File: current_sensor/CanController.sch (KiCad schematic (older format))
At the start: 43 parts, among them P10 CONN_02X03, P7 CONN_01X03, P8 USB, P9 CONN_01X02, SW1 RESET, SW2 BOOT, U6 STM32F042C6, U7 mcp2562

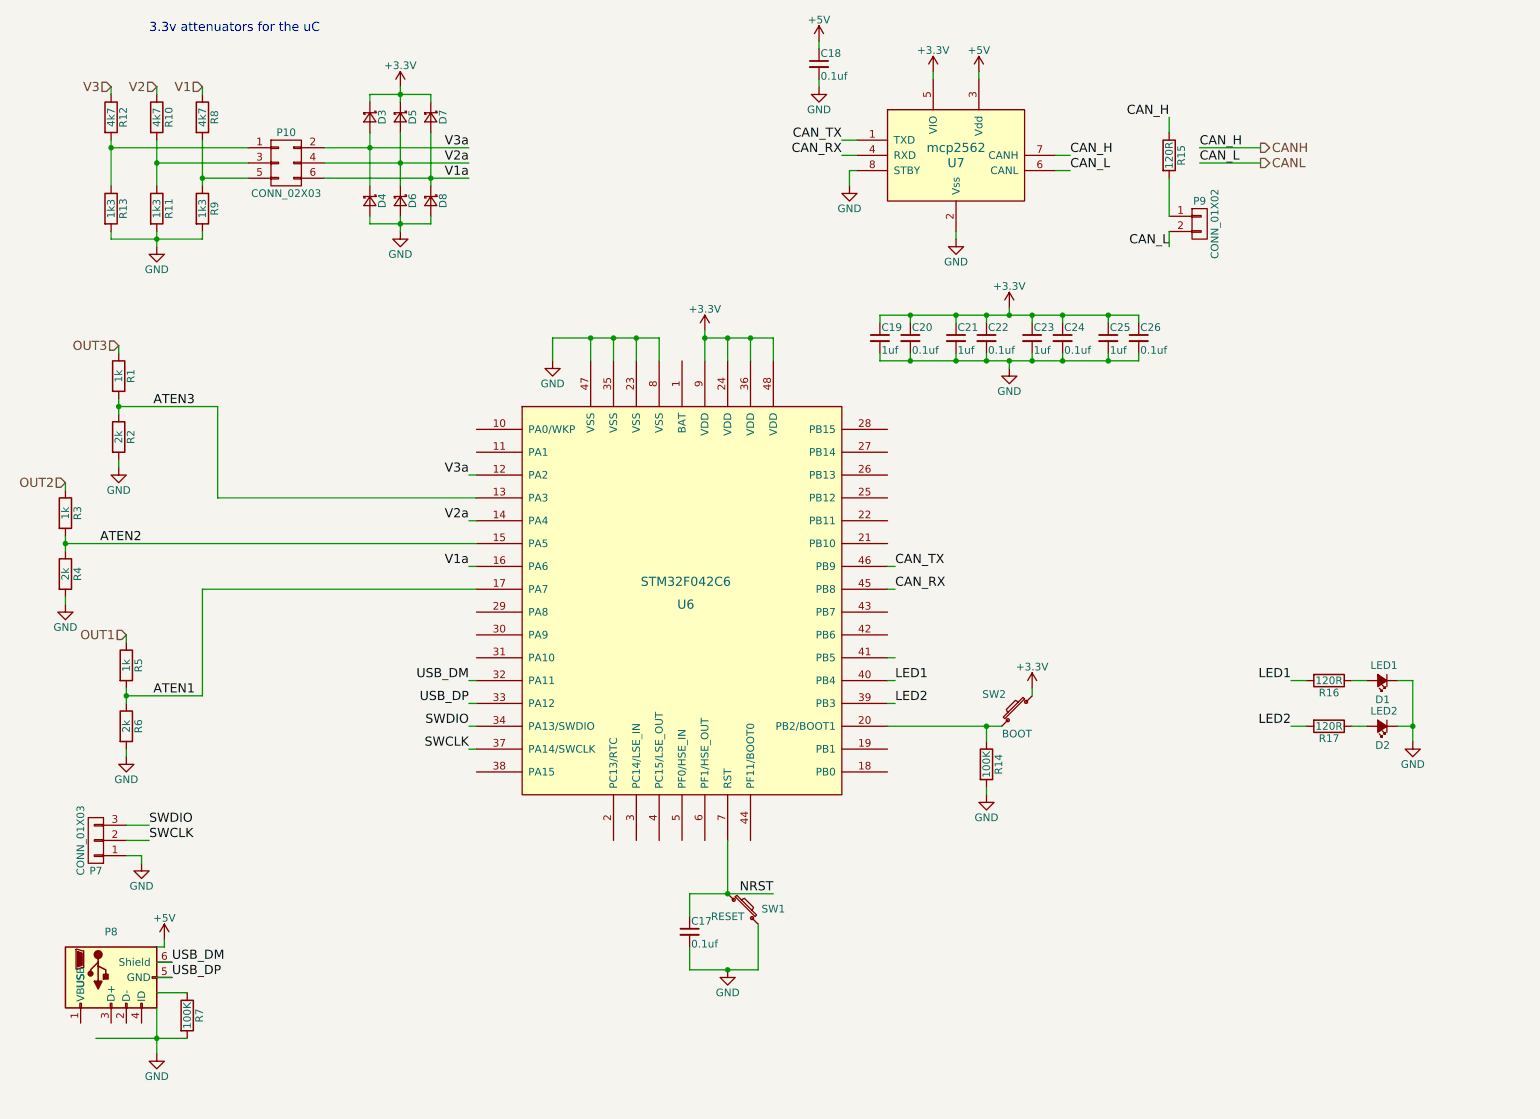
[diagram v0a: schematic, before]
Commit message: Added all components to the board and finilized placement
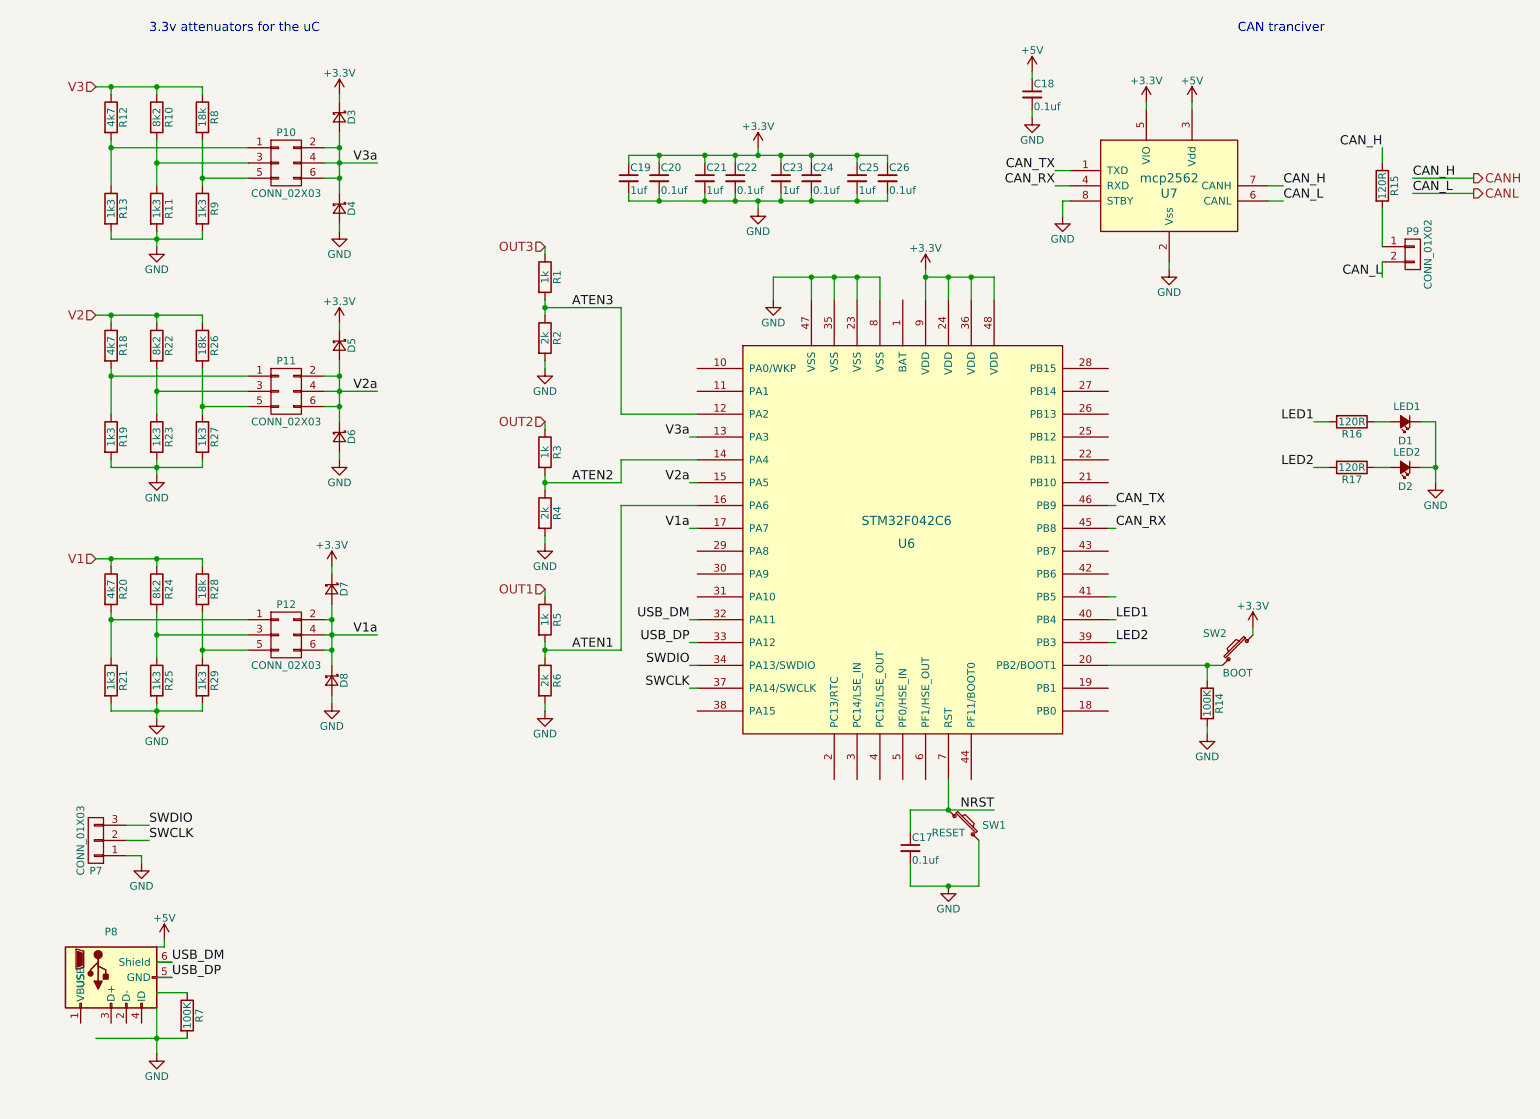
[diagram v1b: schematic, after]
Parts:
- added P11, P12: CONN_02X03, Pin_Headers:Pin_Header_Straight_2x03, symbol CONN_02X03
- added R18, R20: 4k7, Resistors_SMD:R_0603_HandSoldering, symbol R
- added R19, R21, R23, R25, R27, R29: 1k3, Resistors_SMD:R_0603_HandSoldering, symbol R
- added R22, R24: 8k2, Resistors_SMD:R_0603_HandSoldering, symbol R
- added R26, R28: 18k, Resistors_SMD:R_0603_HandSoldering, symbol R
- R10: value 4k7 -> 8k2
- R8: value 4k7 -> 18k; Distributor (none) -> Mouser
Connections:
- wire segments 130 -> 227
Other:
- note added: "CAN tranciver"
- moved on the sheet: C17, C18, C19, C20, C21, C22, C23, C24, C25, C26, D1, D2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

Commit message: added more silkscreen text
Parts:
- D3, D4, D5, D6, D7, D8: Distributor (none) -> Mouser; PN (none) -> 512-SS14FL
- SW1, SW2: footprint Buttons_Switches_SMD:SW_SPST_EVQP0 -> Buttons_Switches_ThroughHole:SW_PUSH_6mm
- U6: Distributor (none) -> Mouser; PN (none) -> 511-STM32F042C6T6
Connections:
- wire segments 227 -> 165
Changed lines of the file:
@@
 F 0 "SW2" H 8650 4960 50  0000 C CNN
 F 1 "BOOT" H 8500 4700 50  0000 C CNN
-F 2 "Buttons_Switches_SMD:SW_SPST_EVQP0" V 8500 4850 50  0001 C CNN
+F 2 "Buttons_Switches_ThroughHole:SW_PUSH_6mm" V 8500 4850 50  0001 C CNN
 F 3 "" H 8500 4850 50  0000 C CNN
 	1    8500 4850
@@
 F 0 "SW1" H 6900 6000 50  0000 C CNN
 F 1 "RESET" H 6600 5950 50  0000 C CNN
-F 2 "Buttons_Switches_SMD:SW_SPST_EVQP0" H 6700 6000 50  0001 C CNN
+F 2 "Buttons_Switches_ThroughHole:SW_PUSH_6mm" H 6700 6000 50  0001 C CNN
 F 3 "" H 6700 6000 50  0000 C CNN
 	1    6700 6000
@@
 F 2 "Housings_QFP:TQFP-48_7x7mm_Pitch0.5mm" H 6300 4100 60  0001 C CNN
 F 3 "" H 6300 4100 60  0000 C CNN
+F 4 "Mouser" H 6300 4100 60  0001 C CNN "Distributor"
+F 5 "511-STM32F042C6T6 " H 6300 4100 60  0001 C CNN "PN"
 	1    6300 4100
 	1    0    0    -1
@@
 F 2 "Diodes_SMD:SOD-123" V 2600 1950 50  0001 C CNN
 F 3 "" V 2600 1950 50  0000 C CNN
+F 4 "Mouser" H 2600 1950 60  0001 C CNN "Distributor"
+F 5 "512-SS14FL " H 2600 1950 60  0001 C CNN "PN"
 	1    2600 1950
 	0    1    1    0
@@
 F 2 "Diodes_SMD:SOD-123" V 2600 1350 50  0001 C CNN
 F 3 "" V 2600 1350 50  0000 C CNN
+F 4 "Mouser" H 2600 1350 60  0001 C CNN "Distributor"
+F 5 "512-SS14FL " H 2600 1350 60  0001 C CNN "PN"
 	1    2600 1350
 	0    1    1    0
@@
 F 2 "Diodes_SMD:SOD-123" V 2600 2850 50  0001 C CNN
 F 3 "" V 2600 2850 50  0000 C CNN
+F 4 "Mouser" H 2600 2850 60  0001 C CNN "Distributor"
+F 5 "512-SS14FL " H 2600 2850 60  0001 C CNN "PN"
 	1    2600 2850
 	0    1    1    0
 $EndComp
 Wire Wire Line
-	6450 2350 6450 2400
-Wire Wire Line
-	6450 2400 6450 2550
-Wire Wire Line
-	6450 2400 6600 2400
-Wire Wire Line
-	6600 2400 6750 2400
-Wire Wire Line
-	6750 2400 6900 2400
+	6450 2350 6450 2550
+Wire Wire Line
+	6450 2400 6900 2400
 Connection ~ 6450 2400
 Wire Wire Line
@@
 	9700 3350 9800 3350
 Wire Wire Line
-	9800 3350 9800 3650
-Wire Wire Line
-	9800 3650 9800 3750
+	9800 3350 9800 3750
 Wire Wire Line
 	9800 3650 9700 3650
@@
 	1450 6800 1400 6800
 Wire Wire Line
-	1400 7200 1400 7400
-Wire Wire Line
-	1400 7400 1400 7500
-Wire Wire Line
-	1000 7400 1400 7400
-Wire Wire Line
-	1400 7400 1600 7400
+	1400 7200 1400 7500
+Wire Wire Line
+	1000 7400 1600 7400
 Connection ~ 1400 7400
 Wire Wire Line
@@
 	6350 6250 6350 6400
 Wire Wire Line
-	7650 4950 8300 4950
-Wire Wire Line
-	8300 4950 8400 4950
+	7650 4950 8400 4950
 Wire Wire Line
 	8300 5050 8300 4950
@@
 	6000 1600 6000 1650
 Wire Wire Line
-	6350 5900 6600 5900
-Wire Wire Line
-	6600 5900 6900 5900
+	6350 5900 6900 5900
 Wire Wire Line
 	6200 1600 6200 1650
@@
 	5450 2550 5450 2400
 Wire Wire Line
-	5450 2400 5700 2400
-Wire Wire Line
-	5700 2400 5850 2400
-Wire Wire Line
-	5850 2400 6000 2400
-Wire Wire Line
-	6000 2400 6150 2400
+	5450 2400 6150 2400
 Wire Wire Line
 	5700 2400 5700 2550
@@
 	6800 6400 6800 6100
 Wire Wire Line
-	6350 6400 6600 6400
-Wire Wire Line
-	6600 6400 6800 6400
+	6350 6400 6800 6400
 Connection ~ 6600 6400
 Wire Wire Line
@@
 	4500 1650 4500 1600
 Wire Wire Line
-	4500 1600 4700 1600
-Wire Wire Line
-	4700 1600 5000 1600
-Wire Wire Line
-	5000 1600 5200 1600
-Wire Wire Line
-	5200 1600 5350 1600
-Wire Wire Line
-	5350 1600 5500 1600
-Wire Wire Line
-	5500 1600 5700 1600
-Wire Wire Line
-	5700 1600 6000 1600
-Wire Wire Line
-	6000 1600 6200 1600
+	4500 1600 6200 1600
 Wire Wire Line
 	4700 1650 4700 1600
@@
 	6200 1900 6200 1850
 Wire Wire Line
-	4500 1900 4700 1900
-Wire Wire Line
-	4700 1900 5000 1900
-Wire Wire Line
-	5000 1900 5200 1900
-Wire Wire Line
-	5200 1900 5350 1900
-Wire Wire Line
-	5350 1900 5500 1900
-Wire Wire Line
-	5500 1900 5700 1900
-Wire Wire Line
-	5700 1900 6000 1900
-Wire Wire Line
-	6000 1900 6200 1900
+	4500 1900 6200 1900
 Wire Wire Line
 	4500 1900 4500 1850
@@
 	3950 2250 3950 2200
 Wire Wire Line
-	3950 2550 3950 2600
-Wire Wire Line
-	3950 2600 3950 2650
+	3950 2550 3950 2650
 Wire Wire Line
 	3950 2950 3950 3000
@@
 	3950 3400 3950 3350
 Wire Wire Line
-	3950 3700 3950 3750
-Wire Wire Line
-	3950 3750 3950 3800
+	3950 3700 3950 3800
 Wire Wire Line
 	3950 4100 3950 4150
@@
 	3950 4500 3950 4450
 Wire Wire Line
-	3950 4800 3950 4850
-Wire Wire Line
-	3950 4850 3950 4900
+	3950 4800 3950 4900
 Wire Wire Line
 	3950 5200 3950 5250
@@
 	1100 2100 1100 2150
 Wire Wire Line
-	1400 2100 1400 2150
-Wire Wire Line
-	1400 2150 1400 2200
+	1400 2100 1400 2200
 Wire Wire Line
 	1700 1150 1700 1200
@@
 F 2 "Diodes_SMD:SOD-123" V 2550 4450 50  0001 C CNN
 F 3 "" V 2550 4450 50  0000 C CNN
+F 4 "Mouser" H 2550 4450 60  0001 C CNN "Distributor"
+F 5 "512-SS14FL " H 2550 4450 60  0001 C CNN "PN"
 	1    2550 4450
 	0    1    1    0
@@
 	4450 2600 4450 3300
 Wire Wire Line
-	1100 2150 1400 2150
-Wire Wire Line
-	1400 2150 1700 2150
+	1100 2150 1700 2150
 Connection ~ 1400 2150
 Wire Wire Line
-	1100 1500 1100 1550
-Wire Wire Line
-	1100 1550 1100 1800
-Wire Wire Line
-	1400 1500 1400 1650
-Wire Wire Line
-	1400 1650 1400 1800
-Wire Wire Line
-	1700 1500 1700 1750
-Wire Wire Line
-	1700 1750 1700 1800
+	1100 1500 1100 1800
+Wire Wire Line
+	1400 1500 1400 1800
+Wire Wire Line
+	1700 1500 1700 1800
 Wire Wire Line
 	1100 1550 2000 1550
@@
 	1400 2650 1400 2700
 Wire Wire Line
-	1400 3600 1400 3650
-Wire Wire Line
-	1400 3650 1400 3700
+	1400 3600 1400 3700
 Wire Wire Line
 	1700 2650 1700 2700
@@
 $EndComp
 Wire Wire Line
-	1100 3650 1400 3650
-Wire Wire Line
-	1400 3650 1700 3650
+	1100 3650 1700 3650
 Connection ~ 1400 3650
 Wire Wire Line
-	1100 3000 1100 3050
-Wire Wire Line
-	1100 3050 1100 3300
-Wire Wire Line
-	1400 3000 1400 3150
-Wire Wire Line
-	1400 3150 1400 3300
-Wire Wire Line
-	1700 3000 1700 3250
-Wire Wire Line
-	1700 3250 1700 3300
+	1100 3000 1100 3300
+Wire Wire Line
+	1400 3000 1400 3300
+Wire Wire Line
+	1700 3000 1700 3300
 Wire Wire Line
 	1100 3050 2000 3050
@@
 	1400 4250 1400 4300
 Wire Wire Line
-	1400 5200 1400 5250
-Wire Wire Line
-	1400 5250 1400 5300
+	1400 5200 1400 5300
 Wire Wire Line
 	1700 4250 1700 4300
@@
 $EndComp
 Wire Wire Line
-	1100 5250 1400 5250
-Wire Wire Line
-	1400 5250 1700 5250
+	1100 5250 1700 5250
 Connection ~ 1400 5250
 Wire Wire Line
-	1100 4600 1100 4650
-Wire Wire Line
-	1100 4650 1100 4900
-Wire Wire Line
-	1400 4600 1400 4750
-Wire Wire Line
-	1400 4750 1400 4900
-Wire Wire Line
-	1700 4600 1700 4850
-Wire Wire Line
-	1700 4850 1700 4900
+	1100 4600 1100 4900
+Wire Wire Line
+	1400 4600 1400 4900
+Wire Wire Line
+	1700 4600 1700 4900
 Wire Wire Line
 	1100 4650 2000 4650
@@
 Connection ~ 1700 4850
 Wire Wire Line
-	1000 1150 1100 1150
-Wire Wire Line
-	1100 1150 1400 1150
-Wire Wire Line
-	1400 1150 1700 1150
+	1000 1150 1700 1150
 Connection ~ 1400 1150
 Wire Wire Line
@@
 F 2 "Diodes_SMD:SOD-123" V 2600 3450 50  0001 C CNN
 F 3 "" V 2600 3450 50  0000 C CNN
+F 4 "Mouser" H 2600 3450 60  0001 C CNN "Distributor"
+F 5 "512-SS14FL " H 2600 3450 60  0001 C CNN "PN"
 	1    2600 3450
 	0    1    1    0
@@
 F 2 "Diodes_SMD:SOD-123" V 2550 5050 50  0001 C CNN
 F 3 "" V 2550 5050 50  0000 C CNN
+F 4 "Mouser" H 2550 5050 60  0001 C CNN "Distributor"
+F 5 "512-SS14FL " H 2550 5050 60  0001 C CNN "PN"
 	1    2550 5050
 	0    1    1    0
 $EndComp
 Wire Wire Line
-	2500 4750 2550 4750
-Wire Wire Line
-	2550 4750 2850 4750
+	2500 4750 2850 4750
 Wire Wire Line
 	2550 4300 2550 4350
@@
 	2550 4850 2500 4850
 Wire Wire Line
-	2550 4550 2550 4650
-Wire Wire Line
-	2550 4650 2550 4750
-Wire Wire Line
-	2550 4750 2550 4850
-Wire Wire Line
-	2550 4850 2550 4950
+	2550 4550 2550 4950
 Connection ~ 2550 4750
 Wire Wire Line
@@
 Connection ~ 2550 4650
 Wire Wire Line
-	1000 4250 1100 4250
-Wire Wire Line
-	1100 4250 1400 4250
-Wire Wire Line
-	1400 4250 1700 4250
+	1000 4250 1700 4250
 Connection ~ 1100 4250
 Connection ~ 1400 4250
 Wire Wire Line
-	2600 2950 2600 3050
-Wire Wire Line
-	2600 3050 2600 3150
-Wire Wire Line
-	2600 3150 2600 3250
-Wire Wire Line
-	2600 3250 2600 3350
+	2600 2950 2600 3350
 Connection ~ 2600 3250
 Connection ~ 2600 3050
@@
 	2500 3250 2600 3250
 Wire Wire Line
-	2500 3150 2600 3150
-Wire Wire Line
-	2600 3150 2850 3150
+	2500 3150 2850 3150
 Wire Wire Line
 	2500 3050 2600 3050
 Wire Wire Line
-	1000 2650 1100 2650
-Wire Wire Line
-	1100 2650 1400 2650
-Wire Wire Line
-	1400 2650 1700 2650
+	1000 2650 1700 2650
 Connection ~ 1100 2650
 Connection ~ 1400 2650
 Wire Wire Line
-	2600 1450 2600 1550
-Wire Wire Line
-	2600 1550 2600 1650
-Wire Wire Line
-	2600 1650 2600 1750
-Wire Wire Line
-	2600 1750 2600 1850
+	2600 1450 2600 1850
 Wire Wire Line
 	2500 1550 2600 1550
 Connection ~ 2600 1550
 Wire Wire Line
-	2500 1650 2600 1650
-Wire Wire Line
-	2600 1650 2850 1650
+	2500 1650 2850 1650
 Connection ~ 2600 1650
 Wire Wire Line

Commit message: fixed some stuff
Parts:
- SW1, SW2: Distributor (none) -> Mouser; PN (none) -> SKHHPPA010
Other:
- note added: "On chip debugger.\nUse a stm32Nucleo board or stlinkv2."
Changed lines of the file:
@@
 F 2 "Buttons_Switches_ThroughHole:SW_PUSH_6mm" V 8500 4850 50  0001 C CNN
 F 3 "" H 8500 4850 50  0000 C CNN
+F 4 "Mouser" H 8500 4850 60  0001 C CNN "Distributor"
+F 5 "SKHHPPA010 " H 8500 4850 60  0001 C CNN "PN"
 	1    8500 4850
 	-1   0    0    -1
@@
 F 2 "Buttons_Switches_ThroughHole:SW_PUSH_6mm" H 6700 6000 50  0001 C CNN
 F 3 "" H 6700 6000 50  0000 C CNN
+F 4 "Mouser" H 6700 6000 60  0001 C CNN "Distributor"
+F 5 "SKHHPPA010 " H 6700 6000 60  0001 C CNN "PN"
 	1    6700 6000
 	1    0    0    -1
@@
 Wire Wire Line
 	4950 4050 4900 4050
+Text Notes 825  5800 0    60   ~ 0
+On chip debugger.\nUse a stm32Nucleo board or stlinkv2.
 $EndSCHEMATC

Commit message: updated 1593BB-box footprint
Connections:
- wire segments 165 -> 169
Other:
- moved on the sheet: R14, SW2
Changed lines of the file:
@@
 L SW_PUSH_SMALL SW2
 U 1 1 581EFCF0
-P 8500 4850
-F 0 "SW2" H 8650 4960 50  0000 C CNN
-F 1 "BOOT" H 8500 4700 50  0000 C CNN
-F 2 "Buttons_Switches_ThroughHole:SW_PUSH_6mm" V 8500 4850 50  0001 C CNN
-F 3 "" H 8500 4850 50  0000 C CNN
-F 4 "Mouser" H 8500 4850 60  0001 C CNN "Distributor"
-F 5 "SKHHPPA010 " H 8500 4850 60  0001 C CNN "PN"
-	1    8500 4850
+P 7450 5800
+F 0 "SW2" H 7600 5910 50  0000 C CNN
+F 1 "BOOT" H 7450 5650 50  0000 C CNN
+F 2 "Buttons_Switches_ThroughHole:SW_PUSH_6mm" V 7450 5800 50  0001 C CNN
+F 3 "" H 7450 5800 50  0000 C CNN
+F 4 "Mouser" H 7450 5800 60  0001 C CNN "Distributor"
+F 5 "SKHHPPA010 " H 7450 5800 60  0001 C CNN "PN"
+	1    7450 5800
 	-1   0    0    -1
 $EndComp
@@
 L GND #PWR035
 U 1 1 581EFCF1
-P 8300 5400
-F 0 "#PWR035" H 8300 5150 50  0001 C CNN
-F 1 "GND" H 8300 5250 50  0000 C CNN
-F 2 "" H 8300 5400 50  0000 C CNN
-F 3 "" H 8300 5400 50  0000 C CNN
-	1    8300 5400
+P 7250 6350
+F 0 "#PWR035" H 7250 6100 50  0001 C CNN
+F 1 "GND" H 7250 6200 50  0000 C CNN
+F 2 "" H 7250 6350 50  0000 C CNN
+F 3 "" H 7250 6350 50  0000 C CNN
+	1    7250 6350
 	1    0    0    -1
 $EndComp
@@
 L +3.3V #PWR036
 U 1 1 581EFCF2
-P 8600 4700
-F 0 "#PWR036" H 8600 4550 50  0001 C CNN
-F 1 "+3.3V" H 8600 4840 50  0000 C CNN
-F 2 "" H 8600 4700 50  0000 C CNN
-F 3 "" H 8600 4700 50  0000 C CNN
-	1    8600 4700
+P 7550 5650
+F 0 "#PWR036" H 7550 5500 50  0001 C CNN
+F 1 "+3.3V" H 7550 5790 50  0000 C CNN
+F 2 "" H 7550 5650 50  0000 C CNN
+F 3 "" H 7550 5650 50  0000 C CNN
+	1    7550 5650
 	1    0    0    -1
 $EndComp
@@
 L R R14
 U 1 1 581EFCF7
-P 8300 5200
-F 0 "R14" V 8380 5200 50  0000 C CNN
-F 1 "100K" V 8300 5200 50  0000 C CNN
-F 2 "Resistors_SMD:R_0603_HandSoldering" H 8230 5200 50  0001 C CNN
-F 3 "" H 8300 5200 50  0000 C CNN
-F 4 "Mouser" V 8300 5200 60  0001 C CNN "Distributor"
-F 5 "71-CRCW0603-100K-E3" V 8300 5200 60  0001 C CNN "PN"
-	1    8300 5200
+P 7250 6150
+F 0 "R14" V 7350 6150 50  0000 C CNN
+F 1 "100K" V 7150 6150 50  0000 C CNN
+F 2 "Resistors_SMD:R_0603_HandSoldering" H 7180 6150 50  0001 C CNN
+F 3 "" H 7250 6150 50  0000 C CNN
+F 4 "Mouser" V 7250 6150 60  0001 C CNN "Distributor"
+F 5 "71-CRCW0603-100K-E3" V 7250 6150 60  0001 C CNN "PN"
+	1    7250 6150
 	1    0    0    -1
 $EndComp
@@
 	6350 6250 6350 6400
 Wire Wire Line
-	7650 4950 8400 4950
-Wire Wire Line
-	8300 5050 8300 4950
-Connection ~ 8300 4950
-Wire Wire Line
-	8300 5400 8300 5350
-Wire Wire Line
-	8600 4700 8600 4750
+	7250 6000 7250 5900
+Connection ~ 7250 5900
+Wire Wire Line
+	7250 6350 7250 6300
+Wire Wire Line
+	7550 5650 7550 5700
 Connection ~ 6600 5900
 Wire Wire Line
@@
 Text Notes 825  5800 0    60   ~ 0
 On chip debugger.\nUse a stm32Nucleo board or stlinkv2.
+Wire Wire Line
+	7350 5900 7025 5900
+Wire Wire Line
+	7025 5900 7025 5700
+Wire Wire Line
+	7025 5700 6750 5700
+$Comp
+L GND #PWR?
+U 1 1 58806A24
+P 8000 5025
+F 0 "#PWR?" H 8000 4775 50  0001 C CNN
+F 1 "GND" H 8000 4875 50  0000 C CNN
+F 2 "" H 8000 5025 50  0000 C CNN
+F 3 "" H 8000 5025 50  0000 C CNN
+	1    8000 5025
+	1    0    0    -1
+$EndComp
+Wire Wire Line
+	8000 5025 8000 4950
+Wire Wire Line
+	8000 4950 7650 4950
 $EndSCHEMATC

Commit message: updated wiring diagrams
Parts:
- P9: value CONN_01X02 -> Term
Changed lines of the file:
@@
 U 1 1 581EFCEC
 P 1100 7000
+AR Path="/581EFCEC" Ref="P8"  Part="1"
+AR Path="/581EF7A1/581EFCEC" Ref="P8"  Part="1"
 F 0 "P8" V 800 7000 50  0000 C CNN
 F 1 "USB" H 1100 7200 50  0000 C CNN
@@
 P 9650 2250
 F 0 "P9" H 9650 2400 50  0000 C CNN
-F 1 "CONN_01X02" V 9750 2250 50  0000 C CNN
+F 1 "Term" V 9750 2250 50  0000 C CNN
 F 2 "Pin_Headers:Pin_Header_Straight_1x02" H 9650 2250 50  0001 C CNN
 F 3 "" H 9650 2250 50  0000 C CNN
@@
 	7025 5700 6750 5700
 $Comp
-L GND #PWR?
+L GND #PWR053
 U 1 1 58806A24
 P 8000 5025
-F 0 "#PWR?" H 8000 4775 50  0001 C CNN
+F 0 "#PWR053" H 8000 4775 50  0001 C CNN
 F 1 "GND" H 8000 4875 50  0000 C CNN
 F 2 "" H 8000 5025 50  0000 C CNN
